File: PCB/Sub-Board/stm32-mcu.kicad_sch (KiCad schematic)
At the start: 42 parts, among them J2 Conn_01x04_Pin, U2 74HC165, U3 STM32F401VETx, U4 74HC165, U5 74HC165, U6 74HC165, U7 74HC165, Y1 26 MHz

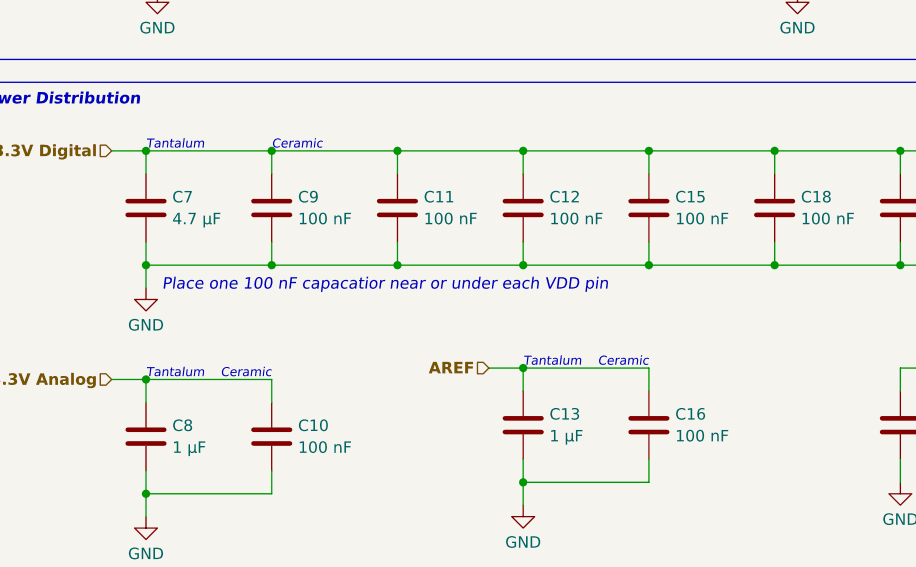
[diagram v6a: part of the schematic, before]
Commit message: Sub Board PCB: Pin Connectors
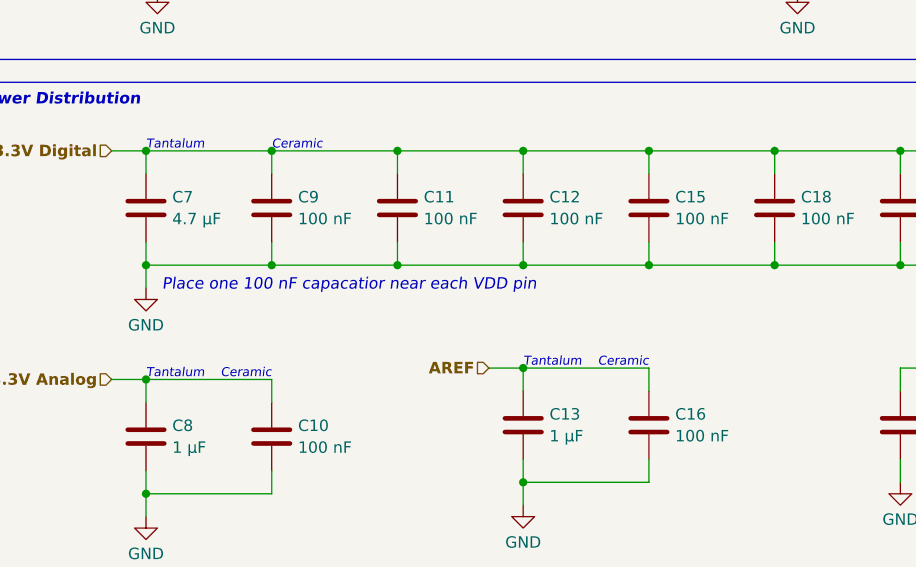
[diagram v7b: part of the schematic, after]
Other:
- note added: "Place one 100 nF capacatior near each VDD pin"
- note removed: "Place one 100 nF capacatior near or under each VDD pin"
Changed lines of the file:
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@@
 		)
 	)
-	(text "Place one 100 nF capacatior near or under each VDD pin"
+	(text "Place one 100 nF capacatior near each VDD pin"
 		(exclude_from_sim no)
 		(at 292.608 132.334 0)

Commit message: Sub Board PCB: GND/GNDD
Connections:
- net GND: no longer C14.2, C17.2, C21.2, C24.2, C3.2, C4.2, C5.2, C6.2, R24.1, U2.10 (DS), U2.15 (~{CE}), U4.15 (~{CE}), U5.15 (~{CE}), U6.15 (~{CE}), U7.15 (~{CE})
- new net GNDD: C14.2, C17.2, C21.2, C24.2, C3.2, C4.2, C5.2, C6.2, R24.1, U2.10 (DS), U2.15 (~{CE}), U4.15 (~{CE}), U5.15 (~{CE}), U6.15 (~{CE}), U7.15 (~{CE})
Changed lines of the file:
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@@
 		(dnp no)
 		(fields_autoplaced yes)
-		(property "Reference" "#PWR027"
+		(property "Reference" "#PWR27"
 			(at 378.46 208.28 0)
 			(effects
@@
 			)
 		)
-		(property "Value" "GND"
+		(property "Value" "GNDD"
 			(at 378.46 206.0631 0)
 			(effects
@@
 			(project ""
 				(path "/f9cf8dcb-b299-4fad-bb24-e1dfd3a00b1a/af464ea0-7d15-463a-8e73-bf1e691932bb"
-					(reference "#PWR027")
+					(reference "#PWR27")
 					(unit 1)
 				)
@@
 		(dnp no)
 		(fields_autoplaced yes)
-		(property "Reference" "#PWR014"
+		(property "Reference" "#PWR14"
 			(at 205.74 99.06 0)
 			(effects
@@
 			)
 		)
-		(property "Value" "GND"
+		(property "Value" "GNDD"
 			(at 205.74 96.8431 0)
 			(effects
@@
 			(project "Template"
 				(path "/f9cf8dcb-b299-4fad-bb24-e1dfd3a00b1a/af464ea0-7d15-463a-8e73-bf1e691932bb"
-					(reference "#PWR014")
+					(reference "#PWR14")
 					(unit 1)
 				)
@@
 		(dnp no)
 		(fields_autoplaced yes)
-		(property "Reference" "#PWR016"
+		(property "Reference" "#PWR16"
 			(at 276.86 99.06 0)
 			(effects
@@
 			)
 		)
-		(property "Value" "GND"
+		(property "Value" "GNDD"
 			(at 276.86 96.8431 0)
 			(effects
@@
 			(project "Template"
 				(path "/f9cf8dcb-b299-4fad-bb24-e1dfd3a00b1a/af464ea0-7d15-463a-8e73-bf1e691932bb"
-					(reference "#PWR016")
+					(reference "#PWR16")
 					(unit 1)
 				)
@@
 		(dnp no)
 		(fields_autoplaced yes)
-		(property "Reference" "#PWR09"
+		(property "Reference" "#PWR9"
 			(at 63.5 99.06 0)
 			(effects
@@
 			)
 		)
-		(property "Value" "GND"
+		(property "Value" "GNDD"
 			(at 63.5 96.8431 0)
 			(effects
@@
 			(project "Template"
 				(path "/f9cf8dcb-b299-4fad-bb24-e1dfd3a00b1a/af464ea0-7d15-463a-8e73-bf1e691932bb"
-					(reference "#PWR09")
+					(reference "#PWR9")
 					(unit 1)
 				)
@@
 		(dnp no)
 		(fields_autoplaced yes)
-		(property "Reference" "#PWR021"
+		(property "Reference" "#PWR21"
 			(at 341.63 208.28 0)
 			(effects
@@
 			)
 		)
-		(property "Value" "GND"
+		(property "Value" "GNDD"
 			(at 341.63 206.0631 0)
 			(effects
@@
 			(project ""
 				(path "/f9cf8dcb-b299-4fad-bb24-e1dfd3a00b1a/af464ea0-7d15-463a-8e73-bf1e691932bb"
-					(reference "#PWR021")
+					(reference "#PWR21")
 					(unit 1)
 				)
@@
 		(dnp no)
 		(fields_autoplaced yes)
-		(property "Reference" "#PWR023"
+		(property "Reference" "#PWR23"
 			(at 360.68 195.58 0)
 			(effects
@@
 			)
 		)
-		(property "Value" "GND"
+		(property "Value" "GNDD"
 			(at 360.68 193.3631 0)
 			(effects
@@
 			(project ""
 				(path "/f9cf8dcb-b299-4fad-bb24-e1dfd3a00b1a/af464ea0-7d15-463a-8e73-bf1e691932bb"
-					(reference "#PWR023")
+					(reference "#PWR23")
 					(unit 1)
 				)
@@
 		(dnp no)
 		(fields_autoplaced yes)
-		(property "Reference" "#PWR012"
+		(property "Reference" "#PWR12"
 			(at 134.62 99.06 0)
 			(effects
@@
 			)
 		)
-		(property "Value" "GND"
+		(property "Value" "GNDD"
 			(at 134.62 96.8431 0)
 			(effects
@@
 			(project "Template"
 				(path "/f9cf8dcb-b299-4fad-bb24-e1dfd3a00b1a/af464ea0-7d15-463a-8e73-bf1e691932bb"
-					(reference "#PWR012")
+					(reference "#PWR12")
 					(unit 1)
 				)
@@
 		(dnp no)
 		(fields_autoplaced yes)
-		(property "Reference" "#PWR022"
+		(property "Reference" "#PWR22"
 			(at 347.98 99.06 0)
 			(effects
@@
 			)
 		)
-		(property "Value" "GND"
+		(property "Value" "GNDD"
 			(at 347.98 96.8431 0)
 			(effects
@@
 			(project "Template"
 				(path "/f9cf8dcb-b299-4fad-bb24-e1dfd3a00b1a/af464ea0-7d15-463a-8e73-bf1e691932bb"
-					(reference "#PWR022")
+					(reference "#PWR22")
 					(unit 1)
 				)
